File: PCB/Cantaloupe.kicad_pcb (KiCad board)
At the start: 2 copper layers, 148.5 x 127.3 mm, 196 parts, among them J1 SWD, J2 USB_In, J3 Split_comm_link, J4 Trackpad, J5 OLED, J6 OLED_PH, Q1 AO3400A, SW1 CPG151101S11, SW10 CPG151101S11, SW11 CPG151101S11, SW12 CPG151101S11, SW13 CPG151101S11, SW14 CPG151101S11, SW15 CPG151101S11, SW16 CPG151101S11, SW17 CPG151101S11, SW18 CPG151101S11, SW19 CPG151101S11, SW2 CPG151101S11, SW20 CPG151101S11, SW21 CPG151101S11, SW22 CPG151101S11, SW23 CPG151101S11, SW24 CPG151101S11, SW25 CPG151101S11, SW26 CPG151101S11, SW27 CPG151101S11, SW28 CPG151101S11, SW29 CPG151101S11, SW3 CPG151101S11, SW30 CPG151101S11, SW31 Encoder, SW32 USB Boot, SW33 Reset, SW4 CPG151101S11, SW5 CPG151101S11, SW6 CPG151101S11, SW7 CPG151101S11, SW8 CPG151101S11, SW9 CPG151101S11, U1 AP2127K-3.3, U2 W25Q128JVS, U3 RP2040, U4 SRV05-4, U5 SRV05-4, U6 PMW3360DM-T2QU, U7 AP2127K-ADJ, Y1 12MHz

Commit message: More routing
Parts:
- removed C19: 4u7, Capacitor_SMD:C_0603_1608Metric
- removed C20: 100n, Capacitor_SMD:C_0402_1005Metric
- removed C24, C5: 1u, Capacitor_SMD:C_0603_1608Metric
- removed JP3: MISO_Pullup, Jumper:SolderJumper-2_P1.3mm_Open_Pad1.0x1.5mm
- removed R13, R15, R16: 10k, Resistor_SMD:R_0402_1005Metric
- removed R14: 39, Resistor_SMD:R_0402_1005Metric
- removed R18: 15k, Resistor_SMD:R_0402_1005Metric
- removed U6: PMW3360DM-T2QU, Cantaloupe:IC_PMW3360DM-T2QU
- removed U7: AP2127K-ADJ, Package_TO_SOT_SMD:SOT-23-5
- added J7: Ogen, Cantaloupe:Ogen-Flippable, F.Cu at (157.1, 107.2)
- A1, JP1: moved to F.Cu
- J6: footprint Cantaloupe:JST_PH_S7B-PH-K_1x07_P2.00mm_Horizontal-Dual -> Cantaloupe:JST_PH_S7B-PH-K_1x07_P2.00mm_Horizontal-Flippable
- SW1, SW10, SW11, SW12, SW13, SW14, SW15, SW16, SW17, SW18, SW19, SW2, SW20, SW21, SW22, SW23, SW24, SW25, SW26, SW27, SW28, SW29, SW3, SW30, SW4, SW5, SW6, SW7, SW8, SW9: footprint Cantaloupe:MX_1U-Hotswap-Dual -> Cantaloupe:MX_1U-Hotswap-Flippable
- SW32: footprint Cantaloupe:SW_DIP_SPSTx01_Slide_6.7x4.1mm_W8.61mm_P2.54mm_LowProfile-Dual -> Cantaloupe:SW_DIP_SPSTx01_Slide_6.7x4.1mm_W8.61mm_P2.54mm_LowProfile-Flippable
- SW33: footprint Cantaloupe:SW_SPST_TL3342-Dual -> Cantaloupe:SW_SPST_TL3342-Flippable; moved to B.Cu
- moved A1 108.3 mm to (93.6, 109.9), turned to 0 degrees
- moved H2 95.8 mm to (21.7, 136.9)
- moved R10 53.7 mm to (150.7, 65.1), turned to 0 degrees
- moved JP1 52.8 mm to (147.8, 65.1), turned to 0 degrees
- moved JP2 51.9 mm to (147.8, 65.1), turned to 0 degrees
- moved Q1 11.2 mm to (139.6, 51.7)
- moved C23 11.0 mm to (143.7, 49.7)
- moved C1 10.5 mm to (68.9, 129.9)
- moved R1 10.5 mm to (67.3, 130.5)
- moved R2 10.5 mm to (68.9, 131.1)
- moved C50 10.4 mm to (122.2, 50.7)
- moved C7 10.4 mm to (155.5, 57.4)
- moved C41 10.4 mm to (93.7, 64.0)
- moved D43 10.4 mm to (69.9, 86.3)
- moved C3 10.4 mm to (139.3, 37.8)
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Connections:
- net Net-(Q1-S) renamed /MCU/RGB_3V3
- U3 pad 14: unconnected-(U3-GPIO11-Pad14) -> /MCU/Side
- U3 pad 27: /MCU/ROTA -> /MCU/ROW4
- U3 pad 28: /MCU/ROTB -> /MCU/ROTA
- U3 pad 29: /MCU/ROW4 -> /MCU/ROTB
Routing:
- net +5V: track 64.5 -> 694.6 mm, vias 16 -> 30
- net Net-(D59-DOUT): track 0.00 -> 47.5 mm, vias 0 -> 2
- net +2V: track 44.7 -> 0.00 mm
- net /Comms/MISO: track 85.7 -> 48.7 mm
- net Net-(D57-DOUT): track 0.00 -> 35.6 mm, vias 0 -> 2
- net Net-(D31-DOUT): track 0.00 -> 31.3 mm
- net Net-(D45-DIN): track 0.00 -> 28.8 mm
- net /MCU/Side: track 0.00 -> 21.1 mm
- net Net-(D49-DOUT): track 0.00 -> 15.8 mm
- net Net-(D48-DIN): track 0.00 -> 15.8 mm
- net Net-(D47-DOUT): track 0.00 -> 15.8 mm
- net Net-(D46-DIN): track 0.00 -> 15.8 mm
- net Net-(D52-DOUT): track 0.00 -> 15.5 mm
- net Net-(D54-DOUT): track 0.00 -> 15.5 mm
- net Net-(D51-DIN): track 0.00 -> 15.5 mm
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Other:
- board size 148.5 x 127.3 mm -> 148.4 x 127.3 mm
- board text added: "3V3"
- board text added: "CLK"
- board text added: "GND"
- board text added: "Jump if LHS"
- board text added: "Jump if RHS"
- board text added: "SWD"

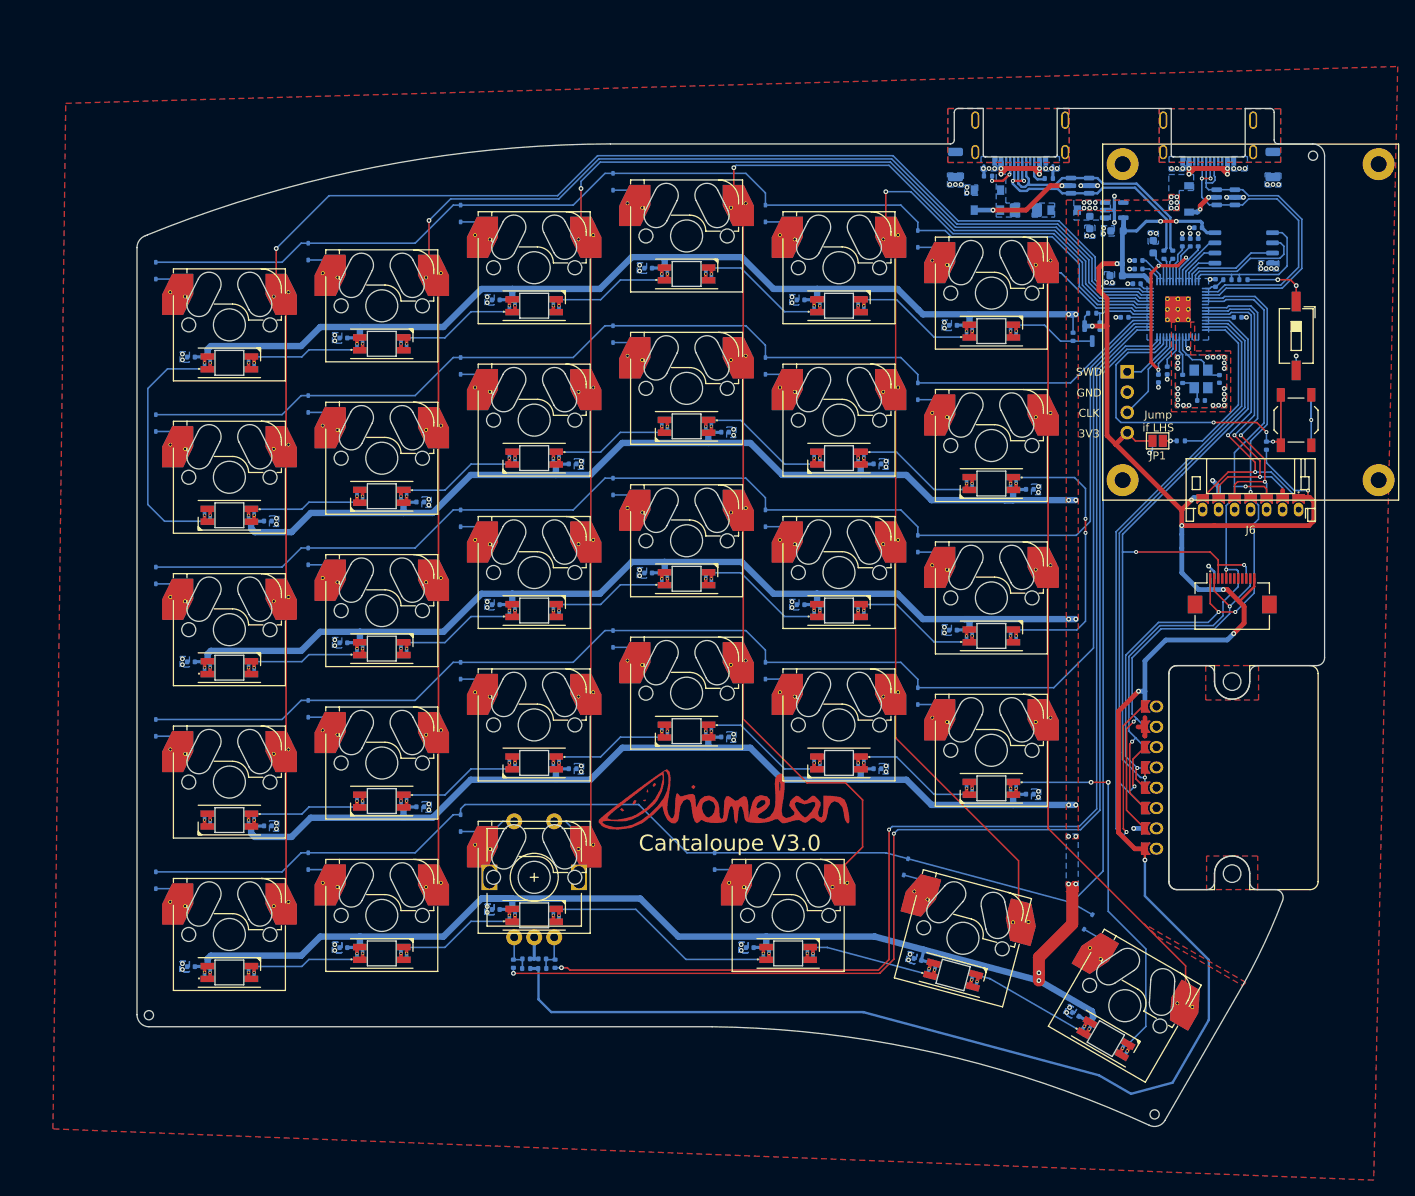
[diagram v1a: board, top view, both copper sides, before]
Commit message: Routing done. Ogen footprint added.
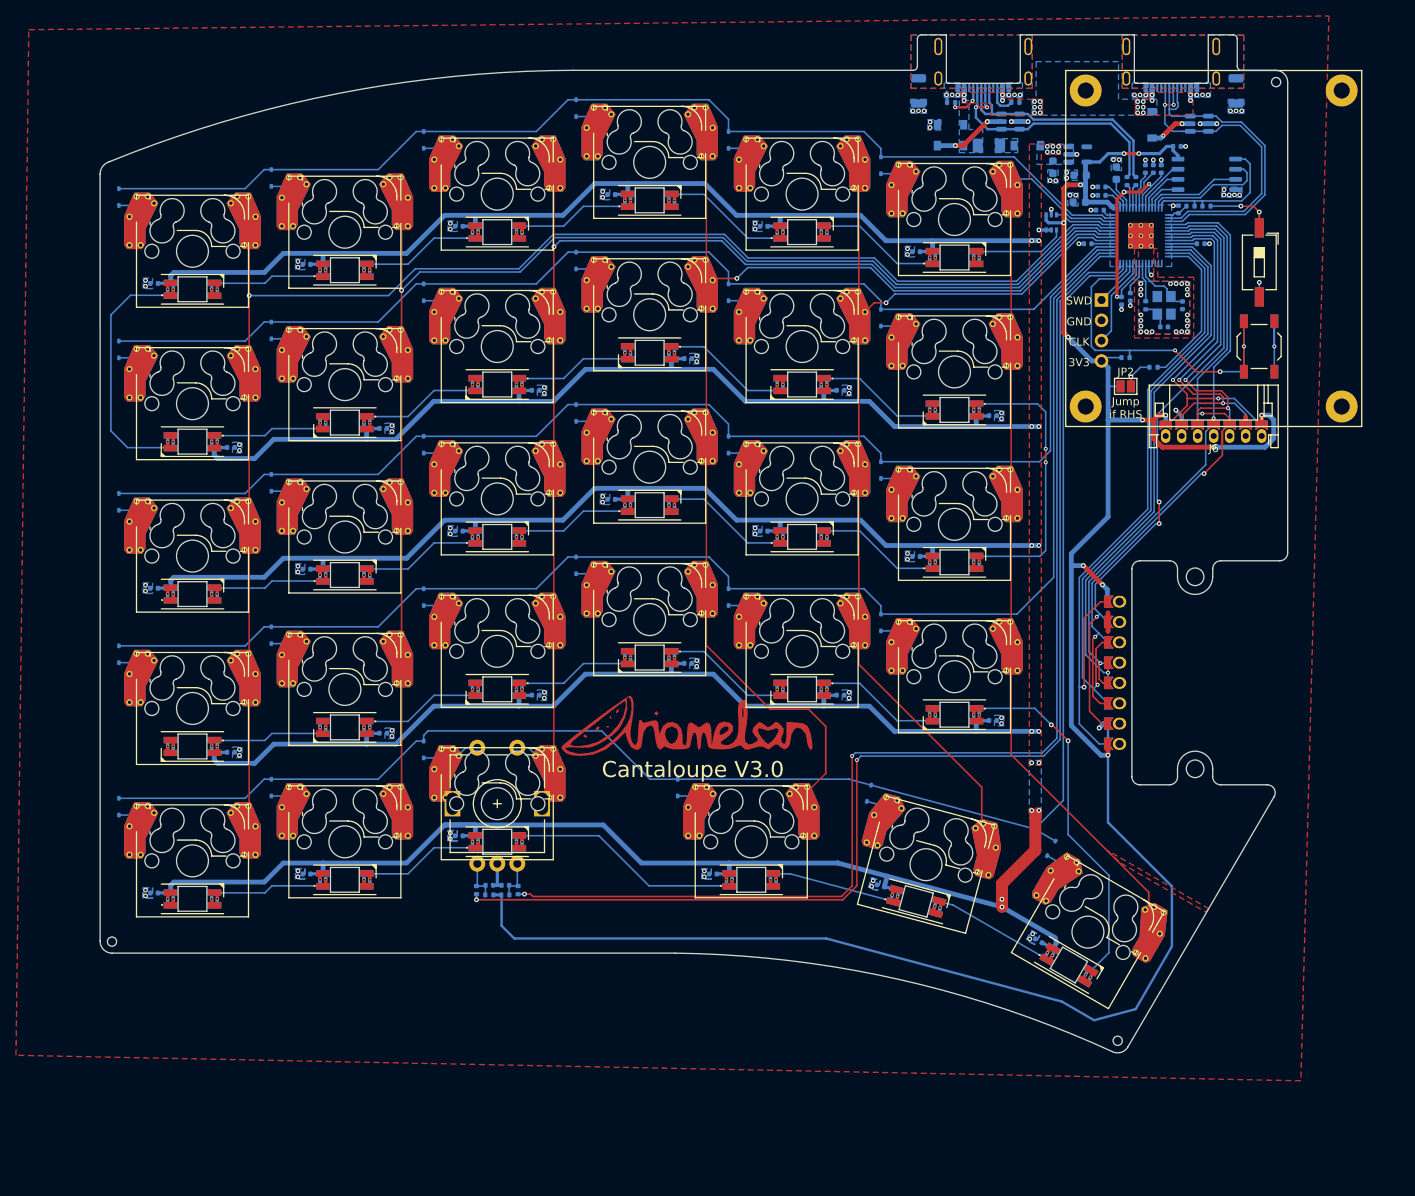
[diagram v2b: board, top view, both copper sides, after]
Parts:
- removed J7: Ogen, Cantaloupe:Ogen-Flippable
- removed Q1: AO3400A, Package_TO_SOT_SMD:SOT-23
- removed R19, R20: 10k, Resistor_SMD:R_0402_1005Metric
- added U6: 74LVC1T45, Package_TO_SOT_SMD:SOT-363_SC-70-6, B.Cu at (134.5, 37.8)
- ?: renamed from J4; value Trackpad -> Ogen; footprint Cantaloupe:Hirose_FH12-12S-0.5SH_1x12-1MP_P0.50mm_Horizontal_Flippable -> Cantaloupe:Ogen-Flippable; moved to F.Cu
- JP1: moved to B.Cu
- JP2: moved to F.Cu
- moved R17 20.8 mm to (143.8, 54.7), turned to 180 degrees
- moved U4 11.8 mm to (129.4, 25.2)
- moved ? 11.0 mm to (152.5, 94.1), turned to 0 degrees
- moved C10 10.8 mm to (143.3, 47.6)
- moved C6 10.5 mm to (150.2, 28.3), turned to 180 degrees
- moved R12 10.4 mm to (130.0, 22.8)
- moved D67 10.3 mm to (147.1, 25.6)
- moved C54 10.3 mm to (132.9, 127.6)
- moved C9 10.3 mm to (148.2, 31.1)
- moved D57 10.3 mm to (122.4, 61.2)
- moved H3 10.3 mm to (142.8, 140.1)
- moved J6 10.3 mm to (160.8, 64.5)
- moved R5 10.3 mm to (151.9, 35.8)
- moved R8 10.3 mm to (145.1, 32.6)
- moved SW27 10.3 mm to (122.4, 56.5)
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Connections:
- ? pad 1: /Comms/SCK -> +3V3
- ? pad 3: /Comms/SS_TB -> /Comms/MOSI
- ? pad 4: unconnected-(J4-Pin_4-Pad4) -> /Comms/SCK
- ? pad 5: /Comms/MOSI -> /Comms/SS_TB
- ? pad 6: unconnected-(J4-Pin_6-Pad6) -> /Comms/MOTION
- ? pad 7: unconnected-(J4-Pin_7-Pad7) -> GND
- ? pad 8: unconnected-(J4-Pin_8-Pad8) -> /Comms/~{RST}_TB
- D67 pad 2: +5V -> VBUS
- J3 pad A4: +5V -> VBUS
- J3 pad A9: +5V -> VBUS
- J3 pad B4: +5V -> VBUS
- J3 pad B9: +5V -> VBUS
- U3 pad 34: /MCU/RGB_3V3 -> /MCU/COL4
- U3 pad 35: /MCU/COL5 -> /MCU/COL3
- U3 pad 36: /MCU/ROW0 -> /MCU/COL2
- U3 pad 37: /MCU/COL4 -> /MCU/COL1
- U3 pad 38: /MCU/COL3 -> /MCU/COL0
- U3 pad 39: /MCU/COL2 -> Net-(U3-GPIO27_ADC1)
- U3 pad 40: /MCU/COL1 -> /MCU/COL5
- U3 pad 41: /MCU/COL0 -> /MCU/ROW0
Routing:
- net /Comms/MISO: track 48.7 -> 78.8 mm, vias 2 -> 3
- net /Comms/SS_TB: track 91.3 -> 67.6 mm, vias 3 -> 1
- net +5V: track 694.6 -> 676.9 mm, vias 30 -> 21
- net +3V3: track 325.5 -> 308.8 mm, vias 11 -> 12
- net /Comms/SCK: track 88.7 -> 74.7 mm, vias 4 -> 2
- net /MCU/COL2: track 166.9 -> 156.1 mm
- net /MCU/COL0: track 203.4 -> 192.9 mm
- net /MCU/COL1: track 183.8 -> 173.4 mm
- net /MCU/COL4: track 134.3 -> 124.4 mm
- net /MCU/COL3: track 157.1 -> 147.8 mm
- net /Comms/~{RST}_TB: track 94.8 -> 86.1 mm
- net /MCU/RGB_3V3: track 8.64 -> 0.00 mm
- net GND: track 47.1 -> 38.9 mm, vias 139 -> 137
- net Net-(U3-GPIO27_ADC1): track 0.00 -> 7.62 mm
- net VBUS: track 17.4 -> 10.0 mm, vias 4 -> 20
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- added copper zone on F.Cu, net VBUS
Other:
- outline, holes or cut-outs redrawn
- board text removed: "OLED"

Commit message: 08/08/2023 update
Removed Ogen footprint, and future VIK support is planned. Rerouted board following latest Honeydew revision. WIP support for the USB2541 is added, but it's very tentative and not yet complete. Added CX70M-24P1 footprint.
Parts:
- removed ?: Ogen, Cantaloupe:Ogen-Flippable
- removed D48, D49, D50, D51, D52, D53, D54, D55, D56, D57, D58, D59, D60: SK6812MINI-E, Cantaloupe:YS-SK6812MINI-E-Flippable
- removed D67, D69, D70: B5819W SL, Cantaloupe:D_SOD-123
- removed D68: SMF5.0A, Cantaloupe:D_SOD-123
- removed F1: nSMD100, Fuse:Fuse_1206_3216Metric
- removed FB2: 60R@100MHz, Inductor_SMD:L_1206_3216Metric
- removed JP2: Side_R, Jumper:SolderJumper-2_P1.3mm_Open_Pad1.0x1.5mm
- removed R10: 1k, Resistor_SMD:R_0402_1005Metric
- removed R11: 5k1, Resistor_SMD:R_0402_1005Metric
- removed R8, R9: 27, Resistor_SMD:R_0402_1005Metric
- removed SW32: USB Boot, Cantaloupe:SW_DIP_SPSTx01_Slide_6.7x4.1mm_W8.61mm_P2.54mm_LowProfile-Flippable
- removed SW33: Reset, Cantaloupe:SW_SPST_TL3342-Flippable
- added A2: VIK Logo, Cantaloupe:vik-logo-medium, F.Cu at (133.8, -28.1)
- added C19: 10n, Capacitor_SMD:C_0402_1005Metric, B.Cu at (216.3, -63.1)
- added C20: 1u, Capacitor_SMD:C_0402_1005Metric, B.Cu at (216.3, -61.1)
- added C24: 100n, Cantaloupe:C_0402_1005Metric, B.Cu at (87.4, 53.7)
- added C5: 1u, Capacitor_SMD:C_0402_1005Metric, B.Cu at (222.0, -61.1)
- added C55: 100n, Cantaloupe:C_0402_1005Metric, B.Cu at (153.6, 64.2)
- added C56: 100n, Cantaloupe:C_0402_1005Metric, B.Cu at (182.6, 87.9)
- added C57: 100n, Cantaloupe:C_0402_1005Metric, B.Cu at (87.4, 129.9)
- added C58: 100n, Cantaloupe:C_0402_1005Metric, B.Cu at (134.5, 60.3)
- added C59: 100n, Cantaloupe:C_0402_1005Metric, B.Cu at (172.6, 105.5)
- added C60: 100n, Cantaloupe:C_0402_1005Metric, B.Cu at (134.5, 98.4)
- added C61: 100n, Cantaloupe:C_0402_1005Metric, B.Cu at (96.4, 107.1)
- added C62: 100n, Cantaloupe:C_0402_1005Metric, B.Cu at (153.6, 102.3)
- added C63: 100n, Cantaloupe:C_0402_1005Metric, B.Cu at (115.5, 102.3)
- added D65: 1N4148, Cantaloupe:D_SOD-323, B.Cu at (209.0, -38.4)
- added D98: 5V, Diode_SMD:D_SOD-523, B.Cu at (333.5, -84.6)
- added H10: M3, Cantaloupe:MountingHole_3.2mm_M3_Pad, B.Cu at (200.3, -57.3)
- added H11: M3, Cantaloupe:MountingHole_3.2mm_M3_Pad, B.Cu at (200.3, -50.1)
- added H14: M2, MountingHole:MountingHole_2.2mm_M2_Pad, B.Cu at (274.8, -10.2)
- added H15: M2, MountingHole:MountingHole_2.2mm_M2_Pad, B.Cu at (274.8, -4.30)
- added H16: M2, MountingHole:MountingHole_2.2mm_M2_Pad, B.Cu at (274.8, 1.65)
- added H17: M2, MountingHole:MountingHole_2.2mm_M2_Pad, B.Cu at (274.8, 7.60)
- added H4: M3, Cantaloupe:MountingHole_3.2mm_M3_Pad, F.Cu at (455.7, 49.8)
- added H5: M3, Cantaloupe:MountingHole_3.2mm_M3_Pad, F.Cu at (105.0, 33.1)
- added H6: M3, Cantaloupe:MountingHole_3.2mm_M3_Pad, B.Cu at (114.1, 130.3)
- added H7: M3, Cantaloupe:MountingHole_3.2mm_M3_Pad, B.Cu at (200.3, -64.4)
- added H8: M3, Cantaloupe:MountingHole_3.2mm_M3_Pad, B.Cu at (268.3, -9.65)
- added H9: M3, Cantaloupe:MountingHole_3.2mm_M3_Pad, B.Cu at (268.3, -2.50)
- added J4: OLED Breakout, Cantaloupe:OLED_1.5_SSD1351_128x128, F.Cu at (209.7, 49.8)
- added Q1: BSS138BKS, Cantaloupe:SOT-363_SC-70-6, B.Cu at (321.1, -75.5)
- added Q2: AO3401A, Cantaloupe:SOT-23-3, B.Cu at (300.4, -58.8)
- added R13: 10k, Resistor_SMD:R_0402_1005Metric, B.Cu at (322.8, -84.7)
- added R14: 15k, Resistor_SMD:R_0402_1005Metric, B.Cu at (320.7, -84.7)
- added R15: 10k, Resistor_SMD:R_0402_1005Metric, B.Cu at (322.8, -83.7)
- added R16: 10k, Resistor_SMD:R_0402_1005Metric, B.Cu at (320.7, -83.7)
- added R18: 10k, Resistor_SMD:R_0402_1005Metric, B.Cu at (323.3, -75.5)
- added R19: 6k8, Resistor_SMD:R_0402_1005Metric, B.Cu at (320.1, -80.2)
- added R20: 2k, Resistor_SMD:R_0402_1005Metric, B.Cu at (320.1, -78.2)
- added R21: 4k7, Resistor_SMD:R_0402_1005Metric, B.Cu at (321.1, -78.2)
- added R22: 2k, Resistor_SMD:R_0402_1005Metric, B.Cu at (322.1, -78.2)
- added R23: 10k, Resistor_SMD:R_0402_1005Metric, B.Cu at (321.1, -73.5)
- added R24: 10k, Resistor_SMD:R_0402_1005Metric, B.Cu at (302.8, -59.3)
- added REF**: HRS_CX70M-24P1, Cantaloupe:HRS_CX70M-24P1, F.Cu at (261.8, 84.3)
- added SW67: PTS645, Cantaloupe:SW_SPST_PTS645, B.Cu at (229.0, -64.1)
- added SW68: PTS645, Cantaloupe:SW_SPST_PTS645, B.Cu at (229.0, -56.2)
- added U10: XC6206P332MR, Cantaloupe:SOT-23-3, B.Cu at (201.3, -42.3)
- added U12: TPD4E05U06, Cantaloupe:USON-10_2.5x1.0mm_P0.5mm, B.Cu at (178.9, 30.5)
- added U8: INA180A4, Package_TO_SOT_SMD:SOT-23-5, B.Cu at (325.9, -86.8)
- added U9: TPS259533, Cantaloupe:WSON-8-1EP_2x2mm_P0.5mm_EP0.9x1.6mm, B.Cu at (322.9, -81.5)
- A1: value Art -> Ariamelon Logo; footprint Cantaloupe:Ariamelon_Logo_x3_CU -> Cantaloupe:Ariamelon_Logo_x3_Mask
- C1, C2: value 10n -> 100n
- C11, C12: value 1u -> 100n; footprint Capacitor_SMD:C_0603_1608Metric -> Capacitor_SMD:C_0402_1005Metric
- C15, C17: value 100n -> 30p
- C18: value 100n -> 470n; footprint Capacitor_SMD:C_0402_1005Metric -> Capacitor_SMD:C_0603_1608Metric
- C22: value 100n -> 10n
- C23: value 100n -> 1u; footprint Capacitor_SMD:C_0402_1005Metric -> Capacitor_SMD:C_0603_1608Metric
- C26, C28, C29, C30: footprint Cantaloupe:C_0402_1005Metric -> Capacitor_SMD:C_0402_1005Metric
- C3: value 4u7 -> 1u; footprint Capacitor_SMD:C_0603_1608Metric -> Capacitor_SMD:C_0402_1005Metric
- C31, C35, C36: value 100n -> 1u; footprint Cantaloupe:C_0402_1005Metric -> Capacitor_SMD:C_0402_1005Metric
- C32, C33, C34: value 100n -> 47u; footprint Cantaloupe:C_0402_1005Metric -> Capacitor_SMD:C_1206_3216Metric
- C7, C8: value 22p -> 100n
- D1, D10, D11, D12, D13, D14, D15, D16, D17, D18, D19, D2, D20, D21, D22, D23, D24, D25, D26, D27, D28, D29, D3, D30, D4, D5, D6, D7, D8, D9: value 1N4148 -> SK6812MINI-E; footprint Cantaloupe:D_SOD-323 -> Cantaloupe:YS-SK6812MINI-E
- D31, D32, D33, D34, D35, D36, D37, D38, D39, D40, D41, D42, D43, D44, D45, D46: value SK6812MINI-E -> BAV70; footprint Cantaloupe:YS-SK6812MINI-E-Flippable -> Cantaloupe:SOT-23-3
- D47: footprint Cantaloupe:YS-SK6812MINI-E-Flippable -> Cantaloupe:YS-SK6812MINI-E
- FB1: value 60R@100MHz -> 50R@100MHz
- H1, H2: moved to B.Cu
- J1: footprint Connector_PinHeader_2.54mm:PinHeader_1x04_P2.54mm_Vertical -> Cantaloupe:Header_SWD
- J2: value USB_In -> TC2030-NL; footprint Cantaloupe:HRO-TYPE-C-31-M-13x -> Connector:Tag-Connect_TC2030-IDC-NL_2x03_P1.27mm_Vertical
- J3: value Split_comm_link -> VIK Keyboard Expansion; footprint Cantaloupe:HRO-TYPE-C-31-M-13x -> Cantaloupe:vik-keyboard-connector-horizontal
- J5: value OLED -> RGB_EX; footprint Cantaloupe:OLED_1.5_SSD1315_128x128_NoPins -> Cantaloupe:Header_RGB; moved to B.Cu
- J6: value OLED_PH -> USB In; footprint Cantaloupe:JST_PH_S7B-PH-K_1x07_P2.00mm_Horizontal-Flippable -> Cantaloupe:HRO-TYPE-C-31-M-13x; moved to B.Cu
- JP1: value Side_L -> RGB_OUT_SEL; footprint Jumper:SolderJumper-2_P1.3mm_Open_Pad1.0x1.5mm -> Jumper:SolderJumper-3_P1.3mm_Open_Pad1.0x1.5mm_NumberLabels
- R12: value 5k1 -> 0.005; footprint Resistor_SMD:R_0402_1005Metric -> Resistor_SMD:R_0805_2012Metric
- R17: value 10k -> 12k
- R2: value 10k -> 1k
- R3, R5: value 10k -> 27
- R7: value 1k -> 1M
- SW1, SW10, SW11, SW12, SW13, SW14, SW15, SW16, SW17, SW18, SW19, SW2, SW20, SW21, SW22, SW23, SW24, SW25, SW26, SW27, SW28, SW29, SW3, SW30, SW4, SW5, SW6, SW7, SW8, SW9: footprint Cantaloupe:MX_1U-Hotswap-Flippable -> Cantaloupe:MXOnly-1U-Hotswap-Flippable
- SW31: value Encoder -> CPG151101S11; footprint Cantaloupe:EC11_Flippable -> Cantaloupe:MXOnly-1U-Hotswap-Flippable; moved to B.Cu
- U1: value AP2127K-3.3 -> ZD25WQ32CEIGR; footprint Package_TO_SOT_SMD:SOT-23-5 -> Cantaloupe:USON-8-1EP_3x2mm_P0.5mm_EP1.6x0.2mm
- U2: value W25Q128JVS -> RP2040; footprint Package_SO:SOIC-8_5.23x5.23mm_P1.27mm -> Cantaloupe:QFN-56-1EP_7x7mm_P0.4mm_EP3.2x3.2mm_ThermalVias
- U3: value RP2040 -> SN74AHCT1G125; footprint Cantaloupe:QFN-56-1EP_7x7mm_P0.4mm_EP3.2x3.2mm_ThermalVias -> Package_TO_SOT_SMD:SOT-353_SC-70-5
- U4: value SRV05-4 -> REF3033; footprint Package_TO_SOT_SMD:SOT-23-6 -> Cantaloupe:SOT-23-3
- U5: value SRV05-4 -> TUSB321; footprint Package_TO_SOT_SMD:SOT-23-6 -> Cantaloupe:Texas_X2QFN-12_1.6x1.6mm_P0.4mm
- U6: value 74LVC1T45 -> 74HC595; footprint Package_TO_SOT_SMD:SOT-363_SC-70-6 -> Cantaloupe:SOIC-16_3.9x9.9mm_P1.27mm
- moved C29 365.6 mm to (325.6, -82.6), turned to 180 degrees
- moved C28 348.6 mm to (323.3, -87.3), turned to 90 degrees
- moved C31 309.5 mm to (324.7, -80.9), turned to 90 degrees
- moved C34 309.4 mm to (299.9, -50.7), turned to 180 degrees
- moved C30 306.3 mm to (320.7, -82.7)
- moved C33 293.1 mm to (299.9, -53.1)
- moved C32 292.4 mm to (299.9, -55.5), turned to 180 degrees
- moved H2 263.9 mm to (195.5, -66.8), turned to 180 degrees
- moved C1 245.2 mm to (222.0, -67.0)
- moved C2 242.4 mm to (222.0, -65.1), turned to 180 degrees
- moved R1 241.2 mm to (213.4, -67.0), turned to 180 degrees
- moved R2 239.1 mm to (213.4, -65.0), turned to 180 degrees
- moved FB1 238.8 mm to (330.7, -87.1), turned to 0 degrees
- moved A1 236.8 mm to (231.5, -88.4)
- moved R3 236.3 mm to (213.4, -63.0), turned to 180 degrees
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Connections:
- C1 pad 2: Net-(C1-Pad2) -> +1V1
- C10 pad 2: +1V1 -> +3V3
- C11 pad 2: +1V1 -> +3V3
- C13 pad 2: +3V3 -> RST
- C15 pad 2: +3V3 -> Net-(U2-XIN)
- C16 pad 2: +3V3 -> +5V
- C17 pad 2: +3V3 -> Net-(C17-Pad2)
- C18 pad 2: +3V3 -> +5V
- C2 pad 2: Net-(C2-Pad2) -> +1V1
- C21 pad 2: +3V3 -> VBUS
- C22 pad 2: +3V3 -> Net-(D98-K)
- C23 pad 1: GND -> VBUS
- C23 pad 2: +3V3 -> GND
- C25 pad 2: +5V -> +5VD
- C26 pad 2: +5V -> +3V3
- C27 pad 2: +5V -> +5VD
- C28 pad 2: +5V -> VBUS
- C29 pad 2: +5V -> /PSU/VBUS_MEAS
- C3 pad 2: +5V -> +1V1
- C30 pad 2: +5V -> Net-(U9-dVdt)
- C31 pad 1: GND -> +5V
- C31 pad 2: +5V -> GND
- C32 pad 1: GND -> +5VD
- C32 pad 2: +5V -> GND
- C33 pad 1: GND -> +5VD
- C33 pad 2: +5V -> GND
- C34 pad 1: GND -> +5VD
- C34 pad 2: +5V -> GND
- C35 pad 1: GND -> +5V
- C35 pad 2: +5V -> GND
- C36 pad 1: GND -> +3V3
- C36 pad 2: +5V -> GND
- C37 pad 2: +5V -> +5VD
- C38 pad 2: +5V -> +5VD
- C39 pad 2: +5V -> +5VD
- C40 pad 2: +5V -> +5VD
- C41 pad 2: +5V -> +5VD
- C42 pad 2: +5V -> +5VD
- C43 pad 2: +5V -> +5VD
- C44 pad 2: +5V -> +5VD
- C45 pad 2: +5V -> +5VD
- C46 pad 2: +5V -> +5VD
- C47 pad 2: +5V -> +5VD
- C48 pad 2: +5V -> +5VD
- C49 pad 2: +5V -> +5VD
- C50 pad 2: +5V -> +5VD
- C51 pad 2: +5V -> +5VD
- C52 pad 2: +5V -> +5VD
- C53 pad 2: +5V -> +5VD
- C54 pad 2: +5V -> +5VD
- C7 pad 2: Net-(U3-XIN) -> +3V3
- C8 pad 2: Net-(C8-Pad2) -> +3V3
- C9 pad 2: +1V1 -> +3V3
- D1 pad 1: /MCU/ROW0 -> +5VD
- D1 pad 2: Net-(D1-A) -> Net-(D1-DOUT)
- D10 pad 1: /MCU/ROW4 -> +5VD
- D10 pad 2: Net-(D10-A) -> Net-(D10-DOUT)
- D11 pad 1: /MCU/ROW0 -> +5VD
- D11 pad 2: Net-(D11-A) -> Net-(D10-DIN)
- D12 pad 1: /MCU/ROW1 -> +5VD
- D12 pad 2: Net-(D12-A) -> Net-(D11-DIN)
- D13 pad 1: /MCU/ROW2 -> +5VD
- D13 pad 2: Net-(D13-A) -> Net-(D13-DOUT)
- D14 pad 1: /MCU/ROW3 -> +5VD
- D14 pad 2: Net-(D14-A) -> Net-(D14-DOUT)
- D15 pad 1: /MCU/ROW4 -> +5VD
- D15 pad 2: Net-(D15-A) -> Net-(D15-DOUT)
- D16 pad 1: /MCU/ROW0 -> +5VD
- D16 pad 2: Net-(D16-A) -> Net-(D16-DOUT)
- D17 pad 1: /MCU/ROW1 -> +5VD
- D17 pad 2: Net-(D17-A) -> Net-(D17-DOUT)
- D18 pad 1: /MCU/ROW2 -> +5VD
- D18 pad 2: Net-(D18-A) -> Net-(D18-DOUT)
- D19 pad 1: /MCU/ROW3 -> +5VD
- D19 pad 2: Net-(D19-A) -> Net-(D19-DOUT)
- D2 pad 1: /MCU/ROW1 -> +5VD
- D2 pad 2: Net-(D2-A) -> Net-(D2-DOUT)
- D20 pad 1: /MCU/ROW4 -> +5VD
- D20 pad 2: Net-(D20-A) -> Net-(D19-DIN)
- D21 pad 1: /MCU/ROW0 -> +5VD
- D21 pad 2: Net-(D21-A) -> Net-(D20-DIN)
- D22 pad 1: /MCU/ROW1 -> +5VD
- D22 pad 2: Net-(D22-A) -> Net-(D21-DIN)
- D23 pad 1: /MCU/ROW2 -> +5VD
- D23 pad 2: Net-(D23-A) -> Net-(D22-DIN)
- D24 pad 1: /MCU/ROW3 -> +5VD
- D24 pad 2: Net-(D24-A) -> Net-(D23-DIN)
- D25 pad 1: /MCU/ROW4 -> +5VD
- D25 pad 2: Net-(D25-A) -> Net-(D25-DOUT)
- D26 pad 1: /MCU/ROW0 -> +5VD
- D26 pad 2: Net-(D26-A) -> Net-(D26-DOUT)
- D27 pad 1: /MCU/ROW1 -> +5VD
- D27 pad 2: Net-(D27-A) -> Net-(D27-DOUT)
- D28 pad 1: /MCU/ROW2 -> +5VD
- D28 pad 2: Net-(D28-A) -> Net-(D28-DOUT)
- D29 pad 1: /MCU/ROW3 -> +5VD
- D29 pad 2: Net-(D29-A) -> Net-(D29-DOUT)
- D3 pad 1: /MCU/ROW2 -> +5VD
- D3 pad 2: Net-(D3-A) -> Net-(D3-DOUT)
- D30 pad 1: /MCU/ROW4 -> +5VD
- D30 pad 2: Net-(D30-A) -> Net-(D30-DOUT)
- D31 pad 1: +5V -> Net-(D31A-A)
- D31 pad 2: Net-(D31-DOUT) -> Net-(D31B-A)
- D31 pad 3: GND -> /MCU/ROW0
- D32 pad 1: +5V -> Net-(D32A-A)
- D32 pad 2: Net-(D32-DOUT) -> Net-(D32B-A)
- D32 pad 3: GND -> /MCU/ROW1
- D33 pad 1: +5V -> Net-(D33A-A)
- D33 pad 2: Net-(D33-DOUT) -> Net-(D33B-A)
- D33 pad 3: GND -> /MCU/ROW2
- D34 pad 1: +5V -> Net-(D34A-A)
- D34 pad 2: Net-(D34-DOUT) -> Net-(D34B-A)
- D34 pad 3: GND -> /MCU/ROW3
- D35 pad 1: +5V -> Net-(D35A-A)
- D35 pad 2: /RGB/RGB_EX -> Net-(D35B-A)
- D35 pad 3: GND -> /MCU/ROW4
- D36 pad 1: +5V -> Net-(D36A-A)
- D36 pad 2: Net-(D31-DIN) -> Net-(D36B-A)
- D36 pad 3: GND -> /MCU/ROW0
- D37 pad 1: +5V -> Net-(D37A-A)
- D37 pad 2: Net-(D37-DOUT) -> Net-(D37B-A)
- D37 pad 3: GND -> /MCU/ROW1
- D38 pad 1: +5V -> Net-(D38A-A)
- D38 pad 2: Net-(D33-DIN) -> Net-(D38B-A)
- D38 pad 3: GND -> /MCU/ROW2
- D39 pad 1: +5V -> Net-(D39A-A)
- D39 pad 2: Net-(D39-DOUT) -> Net-(D39B-A)
- D39 pad 3: GND -> /MCU/ROW3
- D4 pad 1: /MCU/ROW3 -> +5VD
- D4 pad 2: Net-(D4-A) -> Net-(D4-DOUT)
- D40 pad 1: +5V -> Net-(D40A-A)
- D40 pad 2: Net-(D35-DIN) -> Net-(D40B-A)
- D40 pad 3: GND -> /MCU/ROW4
- D41 pad 1: +5V -> Net-(D41A-A)
- D41 pad 2: Net-(D36-DIN) -> Net-(D41B-A)
- D41 pad 3: GND -> /MCU/ROW0
- D42 pad 1: +5V -> Net-(D42A-A)
- D42 pad 2: Net-(D42-DOUT) -> Net-(D42B-A)
- D42 pad 3: GND -> /MCU/ROW1
- D43 pad 1: +5V -> Net-(D43A-A)
- D43 pad 2: Net-(D38-DIN) -> Net-(D43B-A)
- D43 pad 3: GND -> /MCU/ROW2
- D44 pad 1: +5V -> Net-(D44A-A)
- D44 pad 2: Net-(D44-DOUT) -> Net-(D44B-A)
- D44 pad 3: GND -> /MCU/ROW3
- D45 pad 1: +5V -> Net-(D45A-A)
- D45 pad 2: Net-(D40-DIN) -> Net-(D45B-A)
- D45 pad 3: GND -> /MCU/ROW4
- D46 pad 1: +5V -> Net-(D46A-A)
- D46 pad 2: Net-(D41-DIN) -> (no net)
- D46 pad 3: GND -> /MCU/ROW4
- D47 pad 1: +5V -> +5VD
- D47 pad 4: Net-(D42-DOUT) -> Net-(D30-DOUT)
- D5 pad 1: /MCU/ROW4 -> +5VD
- D5 pad 2: Net-(D5-A) -> Net-(D5-DOUT)
- D6 pad 1: /MCU/ROW0 -> +5VD
- D6 pad 2: Net-(D6-A) -> Net-(D12-DIN)
- D7 pad 1: /MCU/ROW1 -> +5VD
- D7 pad 2: Net-(D7-A) -> Net-(D13-DIN)
- D8 pad 1: /MCU/ROW2 -> +5VD
- D8 pad 2: Net-(D8-A) -> Net-(D7-DIN)
- D9 pad 1: /MCU/ROW3 -> +5VD
- D9 pad 2: Net-(D9-A) -> Net-(D8-DIN)
- FB1 pad 1: Net-(J2-SHIELD) -> VBUS
- FB1 pad 2: GND -> Net-(D98-K)
- J1 pad 1: Net-(J1-Pin_1) -> SWD
- J1 pad 3: Net-(J1-Pin_3) -> SWC
- JP1 pad 1: +3V3 -> /MCU/RGB_IN
- JP1 pad 2: Net-(JP1-B) -> Net-(D47-DOUT)
- R1 pad 1: Net-(C1-Pad2) -> +3V3
- R1 pad 2: /MCU/ROTA -> FLASH_CS
- R12 pad 1: GND -> /PSU/VBUS_MEAS
- R12 pad 2: Net-(J2-CC2) -> VBUS
- R17 pad 1: Net-(SW33-B) -> Net-(U9-ILIM)
- R17 pad 2: +3V3 -> GND
- R2 pad 1: Net-(C1-Pad2) -> FLASH_CS
- R2 pad 2: +3V3 -> Net-(SW68-B)
- R3 pad 1: +3V3 -> /MCU/D+
- R3 pad 2: Net-(C2-Pad2) -> Net-(U2-USB_DP)
- R4 pad 1: /MCU/ROTB -> +3V3
- R4 pad 2: Net-(C2-Pad2) -> RST
- R5 pad 1: Net-(U2-~{CS}) -> /MCU/D-
- R5 pad 2: +3V3 -> Net-(U2-USB_DM)
- R6 pad 1: Net-(R6-Pad1) -> Net-(C17-Pad2)
- R6 pad 2: Net-(U2-~{CS}) -> Net-(U2-XOUT)
- R7 pad 1: Net-(C8-Pad2) -> Net-(U5-VBUS_DET)
- R7 pad 2: Net-(U3-XOUT) -> VBUS
- SW1 pad 1: Net-(D1-A) -> COL0
- SW1 pad 2: /MCU/COL0 -> Net-(D31B-A)
- SW10 pad 1: Net-(D10-A) -> Net-(D35A-A)
- SW10 pad 2: /MCU/COL1 -> COL1
- SW11 pad 1: Net-(D11-A) -> COL2
- SW11 pad 2: /MCU/COL2 -> Net-(D36B-A)
- SW12 pad 1: Net-(D12-A) -> COL2
- SW12 pad 2: /MCU/COL2 -> Net-(D37B-A)
- SW13 pad 1: Net-(D13-A) -> COL2
- SW13 pad 2: /MCU/COL2 -> Net-(D38B-A)
- SW14 pad 1: Net-(D14-A) -> COL2
- SW14 pad 2: /MCU/COL2 -> Net-(D39B-A)
- SW15 pad 1: Net-(D15-A) -> COL2
- SW15 pad 2: /MCU/COL2 -> Net-(D40B-A)
- SW16 pad 1: Net-(D16-A) -> Net-(D36A-A)
- SW16 pad 2: /MCU/COL3 -> COL3
- SW17 pad 1: Net-(D17-A) -> Net-(D37A-A)
- SW17 pad 2: /MCU/COL3 -> COL3
- SW18 pad 1: Net-(D18-A) -> Net-(D38A-A)
- SW18 pad 2: /MCU/COL3 -> COL3
- SW19 pad 1: Net-(D19-A) -> Net-(D39A-A)
- SW19 pad 2: /MCU/COL3 -> COL3
- SW2 pad 1: Net-(D2-A) -> COL0
- SW2 pad 2: /MCU/COL0 -> Net-(D32B-A)
- SW20 pad 1: Net-(D20-A) -> Net-(D40A-A)
- SW20 pad 2: /MCU/COL3 -> COL3
- SW21 pad 1: Net-(D21-A) -> COL4
- SW21 pad 2: /MCU/COL4 -> Net-(D41B-A)
- SW22 pad 1: Net-(D22-A) -> COL4
- SW22 pad 2: /MCU/COL4 -> Net-(D42B-A)
- SW23 pad 1: Net-(D23-A) -> COL4
- SW23 pad 2: /MCU/COL4 -> Net-(D43B-A)
- SW24 pad 1: Net-(D24-A) -> COL4
- SW24 pad 2: /MCU/COL4 -> Net-(D44B-A)
- SW25 pad 1: Net-(D25-A) -> COL4
- SW25 pad 2: /MCU/COL4 -> Net-(D45B-A)
- SW26 pad 1: Net-(D26-A) -> Net-(D41A-A)
- SW26 pad 2: /MCU/COL5 -> COL5
- SW27 pad 1: Net-(D27-A) -> Net-(D42A-A)
- SW27 pad 2: /MCU/COL5 -> COL5
- SW28 pad 1: Net-(D28-A) -> Net-(D43A-A)
- SW28 pad 2: /MCU/COL5 -> COL5
- SW29 pad 1: Net-(D29-A) -> Net-(D44A-A)
- SW29 pad 2: /MCU/COL5 -> COL5
- SW3 pad 1: Net-(D3-A) -> COL0
- SW3 pad 2: /MCU/COL0 -> Net-(D33B-A)
- SW30 pad 1: Net-(D30-A) -> Net-(D45A-A)
- SW30 pad 2: /MCU/COL5 -> COL5
- SW4 pad 1: Net-(D4-A) -> COL0
- SW4 pad 2: /MCU/COL0 -> Net-(D34B-A)
- SW5 pad 1: Net-(D5-A) -> COL0
- SW5 pad 2: /MCU/COL0 -> Net-(D35B-A)
- SW6 pad 1: Net-(D6-A) -> Net-(D31A-A)
- SW6 pad 2: /MCU/COL1 -> COL1
- SW7 pad 1: Net-(D7-A) -> Net-(D32A-A)
- SW7 pad 2: /MCU/COL1 -> COL1
- SW8 pad 1: Net-(D8-A) -> Net-(D33A-A)
- SW8 pad 2: /MCU/COL1 -> COL1
- SW9 pad 1: Net-(D9-A) -> Net-(D34A-A)
- SW9 pad 2: /MCU/COL1 -> COL1
- U1 pad 1: +5V -> FLASH_CS
- U1 pad 2: GND -> FLASH_SD1
- U1 pad 3: +5V -> FLASH_SD2
- U1 pad 4: unconnected-(U1-NC-Pad4) -> GND
- U1 pad 5: +3V3 -> FLASH_SD0
- U2 pad 1: Net-(U2-~{CS}) -> +3V3
- U2 pad 2: Net-(U2-DO(IO1)) -> /MCU/TUSB_OUT2
- U2 pad 3: Net-(U2-IO2) -> /MCU/TUSB_OUT1
- U2 pad 4: GND -> unconnected-(U2-GPIO2-Pad4)
- U2 pad 5: Net-(U2-DI(IO0)) -> unconnected-(U2-GPIO3-Pad5)
- U2 pad 6: Net-(U2-CLK) -> /MCU/ROW0
- U2 pad 7: Net-(U2-IO3) -> /MCU/ROW1
- U2 pad 8: +3V3 -> /MCU/ROW2
- U3 pad 1: +3V3 -> GND
- U3 pad 2: /Comms/RX -> RGB_3V3
- U3 pad 3: /Comms/TX -> GND
- U3 pad 4: /Comms/SCK -> /MCU/RGB_OUT
- U3 pad 5: /Comms/MOSI -> +5V
- U4 pad 1: /Comms/D+ -> +5V
- U4 pad 2: GND -> +3V3_REF
- U4 pad 3: /Comms/D- -> GND
- U5 pad 1: /Comms/TX -> CC1
- U5 pad 2: GND -> CC2
- U5 pad 3: /Comms/RX -> unconnected-(U5-CURRENT_MODE-Pad3)
- U5 pad 4: /Comms/RX -> GND
- U5 pad 5: Net-(D67-K) -> Net-(U5-VBUS_DET)
- U5 pad 6: /Comms/TX -> unconnected-(U5-~{VCONN_FAULT}-Pad6)
- U6 pad 1: +3V3 -> COL5
- U6 pad 2: GND -> COL7
- U6 pad 3: Net-(U3-GPIO27_ADC1) -> COL4
- U6 pad 4: /MCU/RGB -> COL3
- U6 pad 5: +5V -> COL2
- U6 pad 6: +5V -> COL1
- Y1 pad 1: Net-(U3-XIN) -> Net-(U2-XIN)
- Y1 pad 3: Net-(C8-Pad2) -> Net-(C17-Pad2)
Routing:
- net +5V: track 676.9 -> 3.73 mm, vias 21 -> 18
- net +5VD: track 0.00 -> 668.7 mm, vias 0 -> 17
- net +3V3: track 308.8 -> 0.00 mm, vias 12 -> 0
- net /MCU/COL0: track 192.9 -> 0.00 mm, vias 1 -> 0
- net /MCU/COL1: track 173.4 -> 0.00 mm, vias 1 -> 0
- net /MCU/COL2: track 156.1 -> 0.00 mm, vias 1 -> 0
- net /MCU/ROTA: track 155.8 -> 0.00 mm, vias 2 -> 0
- net COL0: track 0.00 -> 151.8 mm
- net /MCU/ROTB: track 149.3 -> 0.00 mm, vias 2 -> 0
- net /MCU/COL3: track 147.8 -> 0.00 mm, vias 1 -> 0
- net /MCU/COL4: track 124.4 -> 0.00 mm, vias 1 -> 0
- net /MCU/COL5: track 112.9 -> 0.00 mm
- net COL5: track 0.00 -> 104.7 mm
- net COL4: track 0.00 -> 99.6 mm
- net COL3: track 0.00 -> 90.2 mm
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- added copper zone on B.Cu, net +5VD
- added copper zone on F.Cu, net +5VD
- added copper zone on B.Cu, net /PSU/VBUS_MEAS
- added copper zone on B.Cu, net Net-(D98-K)
- added copper zone on F.Cu, net Net-(D98-K)
- added copper zone on B.Cu, net Net-(U9-ILIM)
- removed copper zone on B.Cu, net +3V3
- removed copper zone on B.Cu, net Net-(D70-A)
- removed copper zone on B.Cu, net Net-(J2-SHIELD)
- removed copper zone on F.Cu, net Net-(J2-SHIELD)
- removed copper zone on B.Cu, net Net-(J3-SHIELD)
- removed copper zone on F.Cu, net Net-(J3-SHIELD)
- removed copper zone on F.Cu, net VBUS
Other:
- board size 148.4 x 127.3 mm -> 155.5 x 134.4 mm
- board text added: "Honeydew V3.0"
- board text added: "J4"
- board text added: "OLED Breakout"
- board text removed: "3V3"
- board text removed: "CLK"
- board text removed: "Cantaloupe V3.0"
- board text removed: "GND"
- board text removed: "Jump if LHS"
- board text removed: "Jump if RHS"
- board text removed: "SWD"
